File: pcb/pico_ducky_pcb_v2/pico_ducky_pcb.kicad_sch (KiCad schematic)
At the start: 31 parts, among them J1 USB_A, SW1 R-667799, SW2 R-667799, U1 MIC5504-3.3YMT, U2 W25Q32JVZP, U3 RP2040, Y1 Crystal_GND24

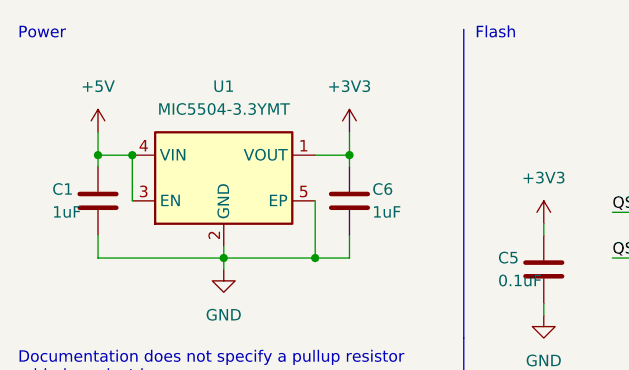
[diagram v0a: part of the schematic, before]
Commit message: add local rp2040, mic5504 symbols and footprints
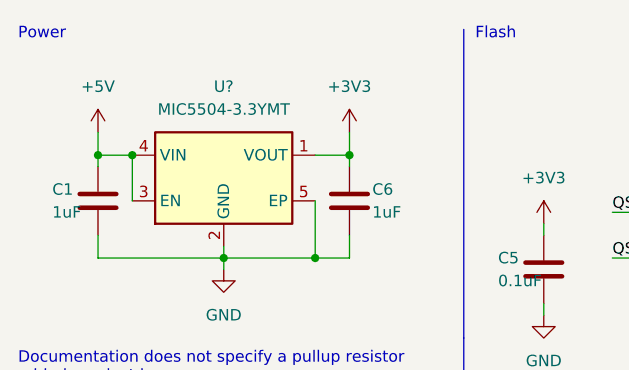
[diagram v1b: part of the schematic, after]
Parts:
- removed U1: MIC5504-3.3YMT, Package_DFN_QFN:UDFN-4-1EP_1x1mm_P0.65mm_EP0.48x0.48mm, symbol MIC5504:MIC5504-3.3YMT
- added U?: MIC5504-3.3YMT, Package_DFN_QFN:UDFN-4-1EP_1x1mm_P0.65mm_EP0.48x0.48mm, symbol MIC5504:MIC5504-3.3YMT
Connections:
- net +3V3: now also U?.1 (VOUT)
- net +5V: now also U?.3 (EN), U?.4 (VIN)
- net GND: now also U?.2 (GND), U?.5 (EP)
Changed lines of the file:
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@@
   (junction (at 72.39 148.59) (diameter 0) (color 0 0 0 0)
   )
+  (junction (at 161.29 185.42) (diameter 0) (color 0 0 0 0)
+  )
+  (junction (at 200.66 43.18) (diameter 0) (color 0 0 0 0)
+  )
+  (junction (at 224.79 43.18) (diameter 0) (color 0 0 0 0)
+  )
+  (junction (at 46.99 160.02) (diameter 0) (color 0 0 0 0)
+  )
+  (junction (at 161.29 182.88) (diameter 0) (color 0 0 0 0)
+  )
+  (junction (at 45.72 38.1) (diameter 0) (color 0 0 0 0)
+  )
+  (junction (at 85.09 171.45) (diameter 0) (color 0 0 0 0)
+  )
+  (junction (at 85.09 160.02) (diameter 0) (color 0 0 0 0)
+  )
+  (junction (at 39.37 171.45) (diameter 0) (color 0 0 0 0)
+  )
   (junction (at 25.4 26.67) (diameter 0) (color 0 0 0 0)
-  )
-  (junction (at 161.29 185.42) (diameter 0) (color 0 0 0 0)
-  )
-  (junction (at 200.66 43.18) (diameter 0) (color 0 0 0 0)
-  )
-  (junction (at 224.79 43.18) (diameter 0) (color 0 0 0 0)
-  )
-  (junction (at 46.99 160.02) (diameter 0) (color 0 0 0 0)
-  )
-  (junction (at 161.29 182.88) (diameter 0) (color 0 0 0 0)
-  )
-  (junction (at 45.72 38.1) (diameter 0) (color 0 0 0 0)
-  )
-  (junction (at 85.09 171.45) (diameter 0) (color 0 0 0 0)
-  )
-  (junction (at 85.09 160.02) (diameter 0) (color 0 0 0 0)
-  )
-  (junction (at 39.37 171.45) (diameter 0) (color 0 0 0 0)
   )
   (junction (at 49.53 26.67) (diameter 0) (color 0 0 0 0)
@@
     (pin "1")
   )
+  (symbol (lib_id "MIC5504:MIC5504-3.3YMT") (at 35.56 29.21 0) (unit 1)
+    (in_bom yes) (on_board yes) (fields_autoplaced)
+    (property "Reference" "U?" (id 0) (at 35.56 19.05 0))
+    (property "Value" "MIC5504-3.3YMT" (id 1) (at 35.56 21.59 0))
+    (property "Footprint" "Package_DFN_QFN:UDFN-4-1EP_1x1mm_P0.65mm_EP0.48x0.48mm" (id 2) (at 35.56 39.37 0)
+      (effects (font (size 1.27 1.27)) hide)
+    )
+    (property "Datasheet" "http://ww1.microchip.com/downloads/en/DeviceDoc/MIC550X.pdf" (id 3) (at 29.21 22.86 0)
+      (effects (font (size 1.27 1.27)) hide)
+    )
+    (pin "1")
+    (pin "2")
+    (pin "3")
+    (pin "4")
+    (pin "5")
+  )
   (symbol (lib_id "Device:R_Small") (at 121.92 172.72 0) (unit 1)
     (in_bom yes) (on_board yes)
@@
     (pin "1")
     (pin "2")
-  )
-  (symbol (lib_id "MIC5504:MIC5504-3.3YMT") (at 35.56 29.21 0) (unit 1)
-    (in_bom yes) (on_board yes) (fields_autoplaced)
-    (property "Reference" "U1" (id 0) (at 35.56 19.05 0))
-    (property "Value" "MIC5504-3.3YMT" (id 1) (at 35.56 21.59 0))
-    (property "Footprint" "Package_DFN_QFN:UDFN-4-1EP_1x1mm_P0.65mm_EP0.48x0.48mm" (id 2) (at 35.56 39.37 0)
-      (effects (font (size 1.27 1.27)) hide)
-    )
-    (property "Datasheet" "http://ww1.microchip.com/downloads/en/DeviceDoc/MIC550X.pdf" (id 3) (at 29.21 22.86 0)
-      (effects (font (size 1.27 1.27)) hide)
-    )
-    (pin "1")
-    (pin "2")
-    (pin "3")
-    (pin "4")
-    (pin "5")
   )
   (symbol (lib_id "MCU_RaspberryPi_RP2040:RP2040") (at 218.44 97.79 0) (unit 1)
@@
       (reference "SW2") (unit 1) (value "R-667799") (footprint "R-WHATEVER:R-667799")
     )
-    (path "/3688ae9f-4d41-4c7d-bd3d-8b45a16022b7"
-      (reference "U1") (unit 1) (value "MIC5504-3.3YMT") (footprint "Package_DFN_QFN:UDFN-4-1EP_1x1mm_P0.65mm_EP0.48x0.48mm")
-    )
     (path "/5c0dfb3e-63f6-4ea6-b3ca-734edf20d662"
       (reference "U2") (unit 1) (value "W25Q32JVZP") (footprint "Package_SON:WSON-8-1EP_6x5mm_P1.27mm_EP3.4x4.3mm")
@@
       (reference "U3") (unit 1) (value "RP2040") (footprint "RP2040_minimal:RP2040-QFN-56")
     )
+    (path "/053463f1-50be-4b2c-90c0-989603a76c05"
+      (reference "U?") (unit 1) (value "MIC5504-3.3YMT") (footprint "Package_DFN_QFN:UDFN-4-1EP_1x1mm_P0.65mm_EP0.48x0.48mm")
+    )
     (path "/3d1c97c4-0ea6-49b5-8e16-2de5448ae48f"

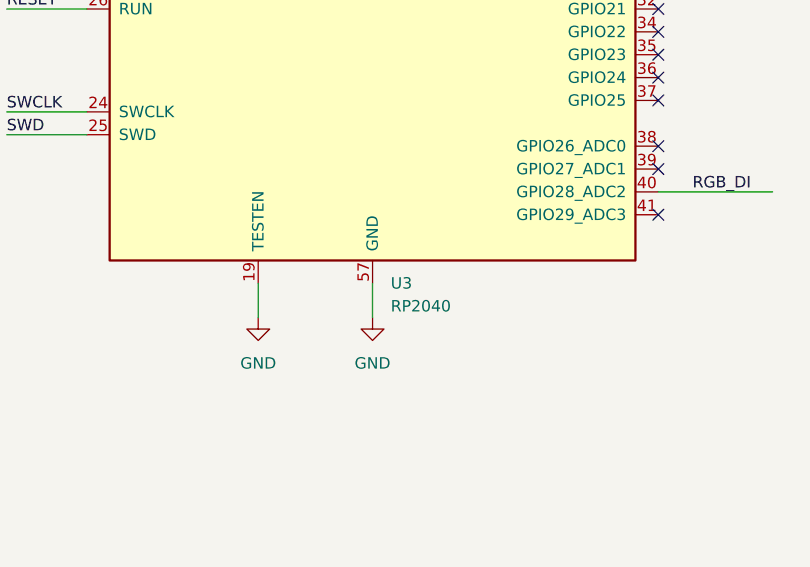
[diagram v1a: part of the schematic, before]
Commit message: update R-667799 kicad footprint
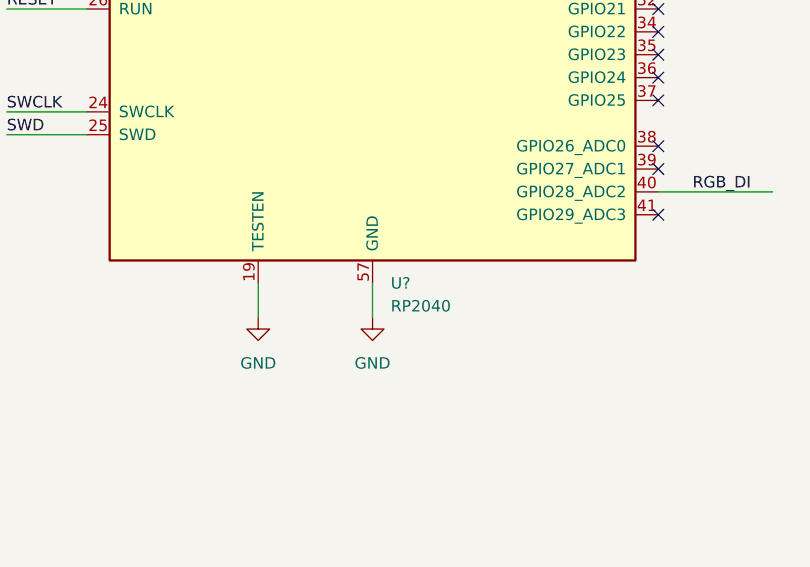
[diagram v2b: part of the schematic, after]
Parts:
- removed U3: RP2040, RP2040_minimal:RP2040-QFN-56, symbol MCU_RaspberryPi_RP2040:RP2040
- added U?: RP2040, RP2040_minimal:RP2040-QFN-56, symbol MCU_RaspberryPi_RP2040:RP2040
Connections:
- net +1V1: now also U?.23 (DVDD), U?.45 (VREG_VOUT), U?.50 (DVDD)
- net +3V3: now also U?.1 (IOVDD), U?.10 (IOVDD), U?.22 (IOVDD), U?.33 (IOVDD), U?.42 (IOVDD), U?.43 (ADC_AVDD), U?.44 (VREG_IN), U?.48 (USB_VDD), U?.49 (IOVDD)
- net GND: now also U?.19 (TESTEN), U?.57 (GND)
- net QSPI_CS: now also U?.56 (QSPI_SS)
- net QSPI_SCLK: now also U?.52 (QSPI_SCLK)
- net QSPI_SD0: now also U?.53 (QSPI_SD0)
- net QSPI_SD1: now also U?.55 (QSPI_SD1)
- net QSPI_SD2: now also U?.54 (QSPI_SD2)
- net QSPI_SD3: now also U?.51 (QSPI_SD3)
- net RESET: now also U?.26 (RUN)
- net RGB_DI: now also U?.40 (GPIO28_ADC2)
- net SWCLK: now also U?.24 (SWCLK)
- net SWD: now also U?.25 (SWD)
- net USBR_+: now also U?.47 (USB_DP)
- net USBR_-: now also U?.46 (USB_DM)
- net X_IN: now also U?.20 (XIN)
- net X_OUT: now also U?.21 (XOUT)
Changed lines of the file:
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@@
-    (pin "2")
-  )
-  (symbol (lib_id "Device:C") (at 46.99 166.37 180) (unit 1)
-    (in_bom yes) (on_board yes)
-    (property "Reference" "C4" (id 0) (at 41.91 165.1 0)
-      (effects (font (size 1.27 1.27)) (justify right))
-    )
-    (property "Value" "0.1uF" (id 1) (at 41.91 167.64 0)
-      (effects (font (size 1.27 1.27)) (justify right))
-    )
-    (property "Footprint" "Capacitor_SMD:C_0201_0603Metric" (id 2) (at 46.0248 162.56 0)
-      (effects (font (size 1.27 1.27)) hide)
-    )
-    (property "Datasheet" "~" (id 3) (at 46.99 166.37 0)
-      (effects (font (size 1.27 1.27)) hide)
-    )
-    (pin "1")
-    (pin "2")
-  )
-  (symbol (lib_id "Device:C") (at 54.61 166.37 180) (unit 1)
-    (in_bom yes) (on_board yes)
-    (property "Reference" "C7" (id 0) (at 49.53 165.1 0)
-      (effects (font (size 1.27 1.27)) (justify right))
-    )
-    (property "Value" "0.1uF" (id 1) (at 49.53 167.64 0)
-      (effects (font (size 1.27 1.27)) (justify right))
-    )
-    (property "Footprint" "Capacitor_SMD:C_0201_0603Metric" (id 2) (at 53.6448 162.56 0)
-      (effects (font (size 1.27 1.27)) hide)
-    )
-    (property "Datasheet" "~" (id 3) (at 54.61 166.37 0)
-      (effects (font (size 1.27 1.27)) hide)
-    )
-    (pin "1")
-    (pin "2")
-  )
-  (symbol (lib_id "Device:C") (at 49.53 31.75 180) (unit 1)
-    (in_bom yes) (on_board yes)
-    (property "Reference" "C6" (id 0) (at 52.07 30.48 0)
-      (effects (font (size 1.27 1.27)) (justify right))
-    )
-    (property "Value" "1uF" (id 1) (at 52.07 33.02 0)
-      (effects (font (size 1.27 1.27)) (justify right))
-    )
-    (property "Footprint" "Capacitor_SMD:C_0402_1005Metric" (id 2) (at 48.5648 27.94 0)
-      (effects (font (size 1.27 1.27)) hide)
-    )
-    (property "Datasheet" "~" (id 3) (at 49.53 31.75 0)
-      (effects (font (size 1.27 1.27)) hide)
-    )
-    (pin "1")
     (pin "2")
   )
   (symbol (lib_id "MCU_RaspberryPi_RP2040:RP2040") (at 218.44 97.79 0) (unit 1)
     (in_bom yes) (on_board yes) (fields_autoplaced)
-    (property "Reference" "U3" (id 0) (at 220.4594 148.59 0)
+    (property "Reference" "U?" (id 0) (at 220.4594 148.59 0)
       (effects (font (size 1.27 1.27)) (justify left))
     )
@@
     (pin "9")
   )
+  (symbol (lib_id "Device:C") (at 46.99 166.37 180) (unit 1)
+    (in_bom yes) (on_board yes)
+    (property "Reference" "C4" (id 0) (at 41.91 165.1 0)
+      (effects (font (size 1.27 1.27)) (justify right))
+    )
+    (property "Value" "0.1uF" (id 1) (at 41.91 167.64 0)
+      (effects (font (size 1.27 1.27)) (justify right))
+    )
+    (property "Footprint" "Capacitor_SMD:C_0201_0603Metric" (id 2) (at 46.0248 162.56 0)
+      (effects (font (size 1.27 1.27)) hide)
+    )
+    (property "Datasheet" "~" (id 3) (at 46.99 166.37 0)
+      (effects (font (size 1.27 1.27)) hide)
+    )
+    (pin "1")
+    (pin "2")
+  )
+  (symbol (lib_id "Device:C") (at 54.61 166.37 180) (unit 1)
+    (in_bom yes) (on_board yes)
+    (property "Reference" "C7" (id 0) (at 49.53 165.1 0)
+      (effects (font (size 1.27 1.27)) (justify right))
+    )
+    (property "Value" "0.1uF" (id 1) (at 49.53 167.64 0)
+      (effects (font (size 1.27 1.27)) (justify right))
+    )
+    (property "Footprint" "Capacitor_SMD:C_0201_0603Metric" (id 2) (at 53.6448 162.56 0)
+      (effects (font (size 1.27 1.27)) hide)
+    )
+    (property "Datasheet" "~" (id 3) (at 54.61 166.37 0)
+      (effects (font (size 1.27 1.27)) hide)
+    )
+    (pin "1")
+    (pin "2")
+  )
+  (symbol (lib_id "Device:C") (at 49.53 31.75 180) (unit 1)
+    (in_bom yes) (on_board yes)
+    (property "Reference" "C6" (id 0) (at 52.07 30.48 0)
+      (effects (font (size 1.27 1.27)) (justify right))
+    )
+    (property "Value" "1uF" (id 1) (at 52.07 33.02 0)
+      (effects (font (size 1.27 1.27)) (justify right))
+    )
+    (property "Footprint" "Capacitor_SMD:C_0402_1005Metric" (id 2) (at 48.5648 27.94 0)
+      (effects (font (size 1.27 1.27)) hide)
+    )
+    (property "Datasheet" "~" (id 3) (at 49.53 31.75 0)
+      (effects (font (size 1.27 1.27)) hide)
+    )
+    (pin "1")
+    (pin "2")
+  )
   (symbol (lib_id "Device:Crystal_GND24") (at 81.28 73.66 0) (unit 1)
     (in_bom yes) (on_board yes) (fields_autoplaced)
@@
       (reference "U2") (unit 1) (value "W25Q32JVZP") (footprint "Package_SON:WSON-8-1EP_6x5mm_P1.27mm_EP3.4x4.3mm")
     )
-    (path "/3a257eca-60b4-402a-98e0-95c5829faabc"
-      (reference "U3") (unit 1) (value "RP2040") (footprint "RP2040_minimal:RP2040-QFN-56")
-    )
     (path "/053463f1-50be-4b2c-90c0-989603a76c05"
       (reference "U?") (unit 1) (value "MIC5504-3.3YMT") (footprint "Package_DFN_QFN:UDFN-4-1EP_1x1mm_P0.65mm_EP0.48x0.48mm")
     )
+    (path "/25231814-4811-4fed-8235-1b554c6e5d8b"
+      (reference "U?") (unit 1) (value "RP2040") (footprint "RP2040_minimal:RP2040-QFN-56")
+    )
     (path "/3d1c97c4-0ea6-49b5-8e16-2de5448ae48f"

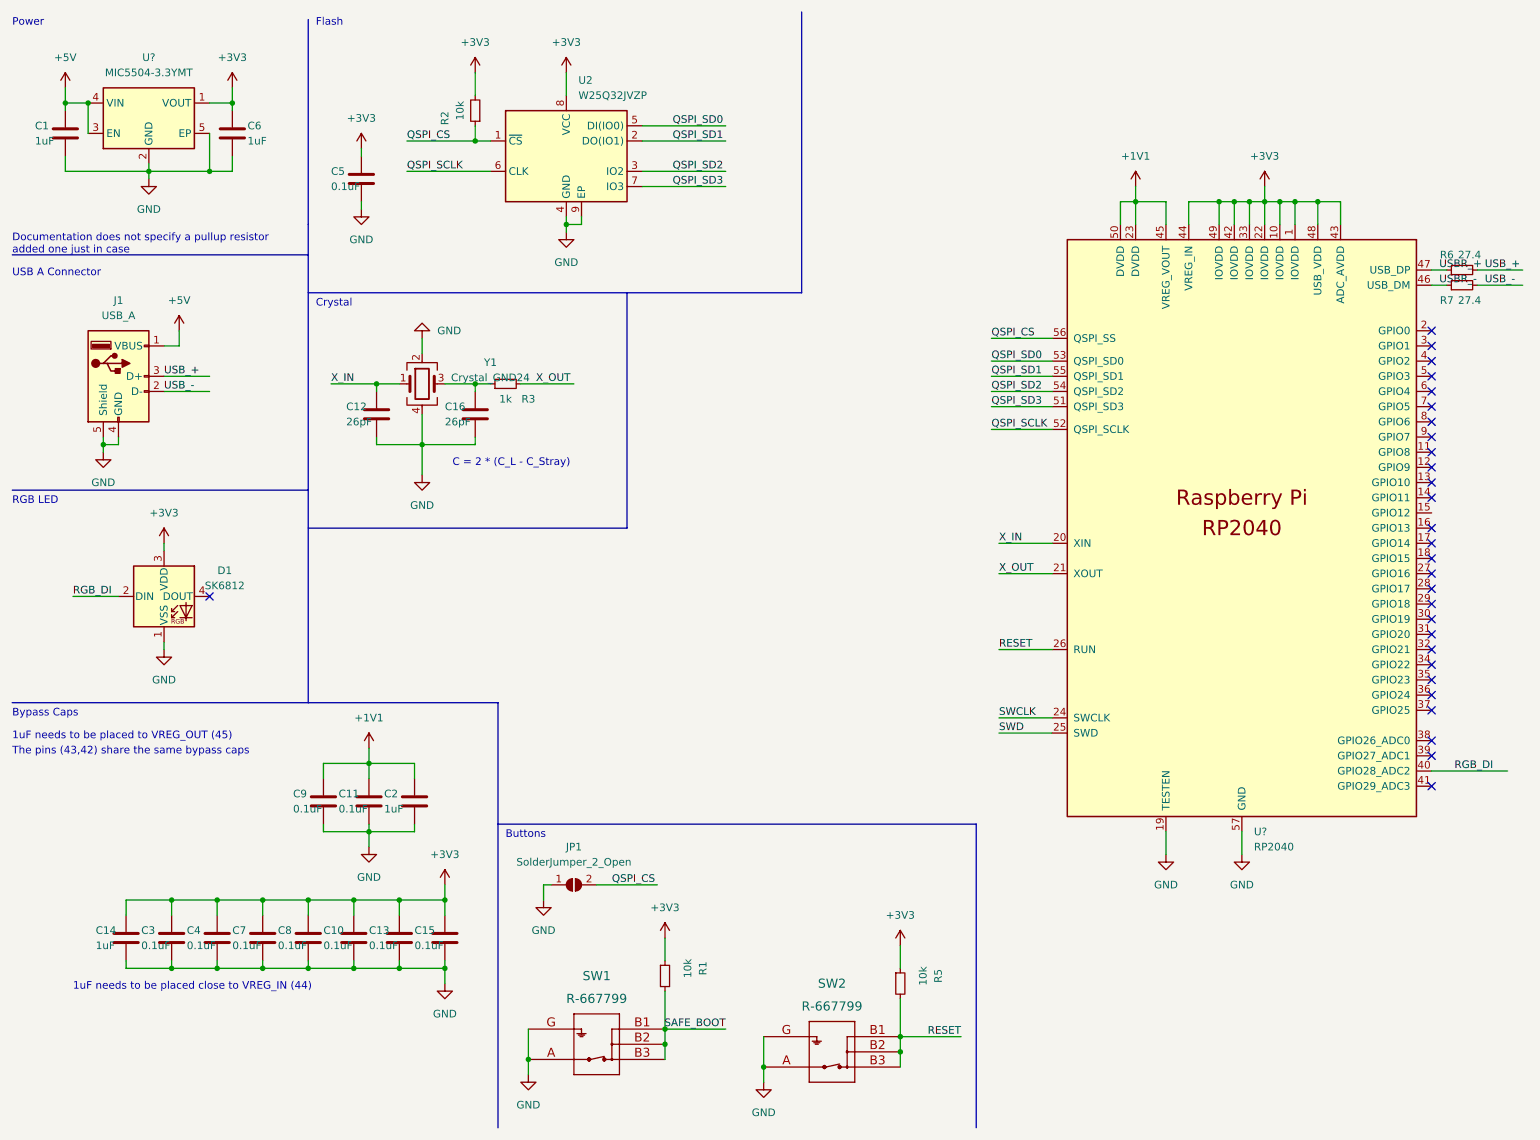
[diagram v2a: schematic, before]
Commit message: update the R-667799 footprint and component finish routing
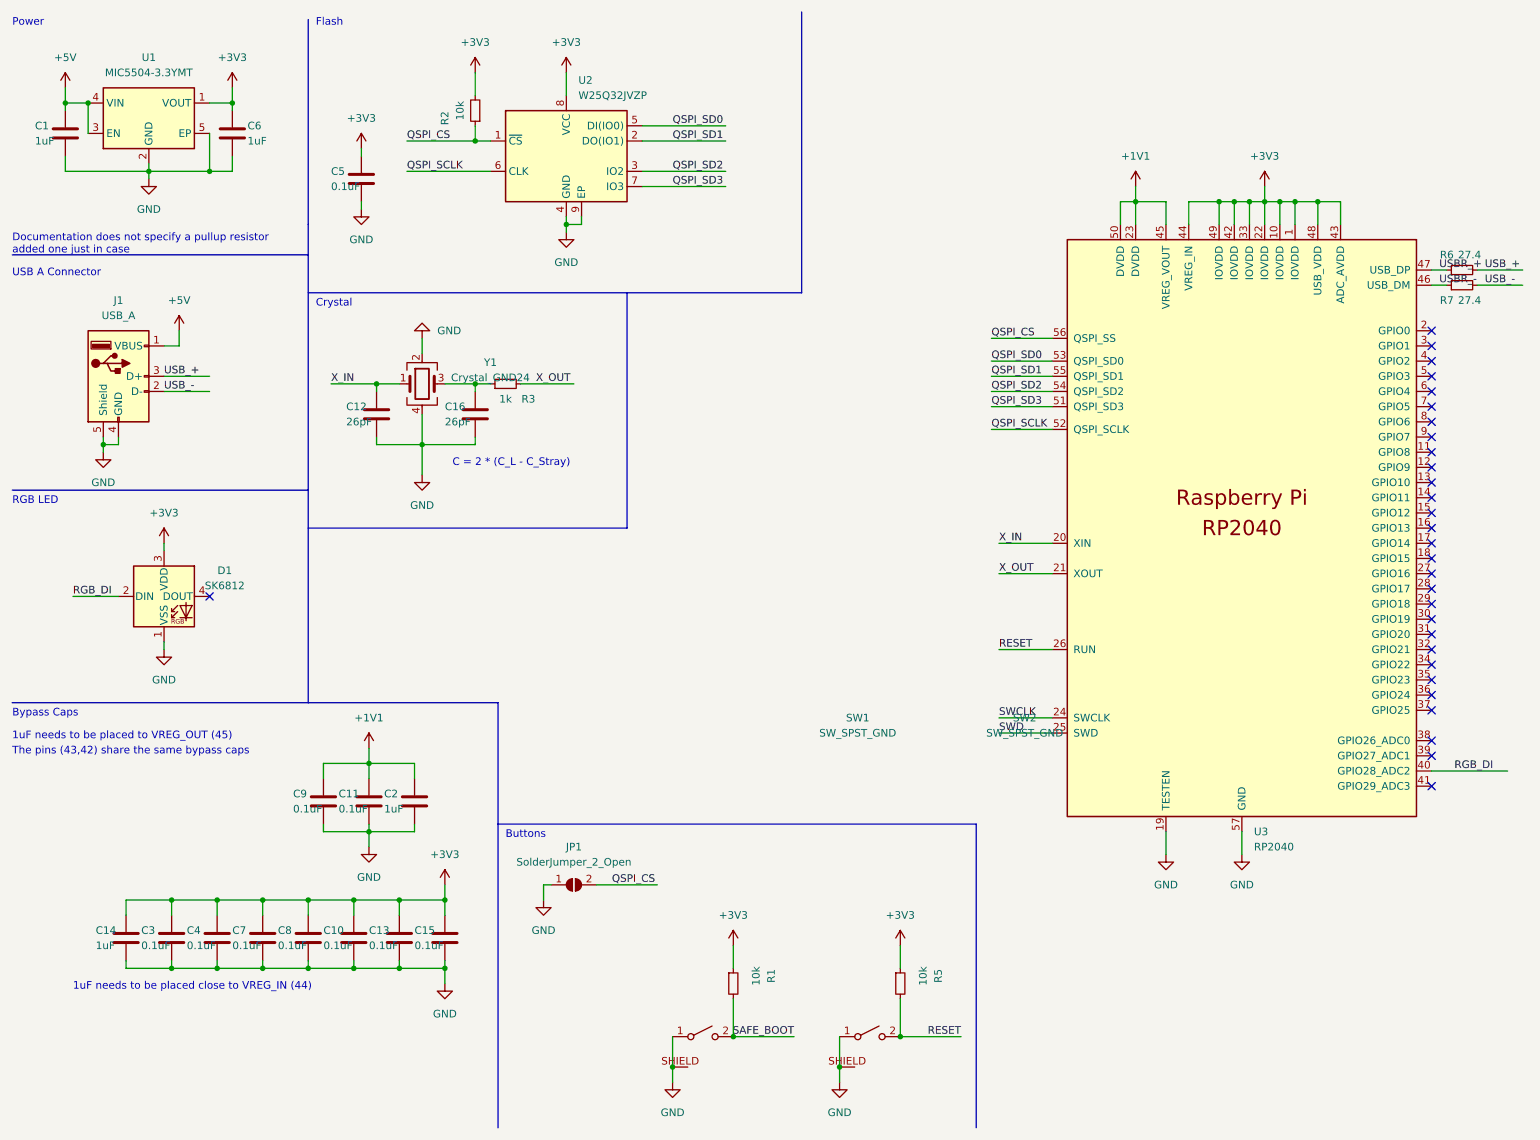
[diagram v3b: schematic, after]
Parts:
- removed SW1, SW2: R-667799, R-WHATEVER:R-667799, symbol 2022-04-30_19-21-11:R-667799
- added SW1, SW2: SW_SPST_GND, pico-ducky-pcb-v2:R-667799, symbol SW_SPST_GND:SW_SPST_GND
- gave numbers to parts that had none: 2
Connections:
- net GND: now also SW1.1 (A), SW1.SHIELD, SW2.1 (A), SW2.SHIELD
- net RESET: now also SW2.2 (B)
- net SAFE_BOOT: now also SW1.2 (B)
- no-connect marks 29 -> 30
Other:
- moved on the sheet: R1

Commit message: use the weurth usb a connector
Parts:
- J1: footprint Connector_USB:USB_A_CNCTech_1001-011-01101_Horizontal -> pico-ducky-pcb-v2:USB3_A_Plug_Wuerth_629004113921_Horizontal
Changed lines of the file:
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@@
     (property "Reference" "J1" (id 0) (at 30.48 59.69 0))
     (property "Value" "USB_A" (id 1) (at 30.48 62.23 0))
-    (property "Footprint" "Connector_USB:USB_A_CNCTech_1001-011-01101_Horizontal" (id 2) (at 34.29 73.66 0)
+    (property "Footprint" "pico-ducky-pcb-v2:USB3_A_Plug_Wuerth_629004113921_Horizontal" (id 2) (at 34.29 73.66 0)
       (effects (font (size 1.27 1.27)) hide)
     )
@@
     )
     (path "/f4221855-6e91-4693-826c-bfa7fd4d2334"
-      (reference "J1") (unit 1) (value "USB_A") (footprint "Connector_USB:USB_A_CNCTech_1001-011-01101_Horizontal")
+      (reference "J1") (unit 1) (value "USB_A") (footprint "pico-ducky-pcb-v2:USB3_A_Plug_Wuerth_629004113921_Horizontal")
     )
     (path "/8c023fa6-4dbe-46d5-bfa7-6ee6396f4a95"

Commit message: WIP
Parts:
- removed SW1, SW2: SW_SPST_GND, pico-ducky-pcb-v2:R-667799, symbol SW_SPST_GND:SW_SPST_GND
- removed U1: MIC5504-3.3YMT, Package_DFN_QFN:UDFN-4-1EP_1x1mm_P0.65mm_EP0.48x0.48mm, symbol MIC5504:MIC5504-3.3YMT
- added SW1, SW2: R-667799, Kevin_Lutzer_Lbr:R-667799, symbol Kevin_Lutzer_Lbr:R-667799
- added U1: TCR2EE33, Package_TO_SOT_SMD:SOT-553, symbol Regulator_Linear:TCR2EE33
- added U4: D1213A-04V, Package_TO_SOT_SMD:SOT-563, symbol Kevin_Lutzer_Lbr:D1213A-04V
- J1: footprint pico-ducky-pcb-v2:USB3_A_Plug_Wuerth_629004113921_Horizontal -> Kevin_Lutzer_Lbr:USB3_A_Plug_Wuerth_629004113921_Horizontal
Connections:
- net +3V3: now also U1.4 (VOUT)
- net +5V: now also U1.1 (CTRL), U1.3 (VIN), U4.2
- net GND: now also SW1.1 (A), SW1.3 (SH), SW2.1 (A), SW2.3 (SH), U1.2 (GND), U4.4, U4.5, U4.6
- net RESET: now also SW2.2 (B)
- net SAFE_BOOT: now also SW1.2 (B)
- net USB_+: now also U4.1
- net USB_-: now also U4.3
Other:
- note added: "C = 2 * (C_L - C_Stray) C_Stray = few pF"
- note removed: "C = 2 * (C_L - C_Stray)"
- company: (none) -> Kevin Lutzer
- title: (none) -> RP2040 Rubber Ducky
- moved on the sheet: J1, R1, R5
